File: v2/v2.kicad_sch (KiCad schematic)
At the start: 65 parts, among them J1 rBUSoutV, J10 mcuTIEout, J2 rBUSinV, J3 cTIEoutV, J4 cTIEinV, J5 cBUSoutH, J6 cTIEoutH, J7 mcuTIEin, J8 cTIEinH, J9 cBUSinH, SW1 KeySwitch, SW10 KeySwitch, SW11 KeySwitch, SW12 KeySwitch, SW13 KeySwitch, SW14 KeySwitch, SW15 KeySwitch, SW16 KeySwitch, SW17 KeySwitch, SW18 KeySwitch, SW19 KeySwitch, SW2 KeySwitch, SW20 KeySwitch, SW21 KeySwitch, SW22 KeySwitch, SW23 KeySwitch, SW24 KeySwitch, SW25 KeySwitch, SW3 KeySwitch, SW4 KeySwitch, SW5 KeySwitch, SW6 KeySwitch, SW7 KeySwitch, SW8 KeySwitch, SW9 KeySwitch, U1 ItsyBitsy5V

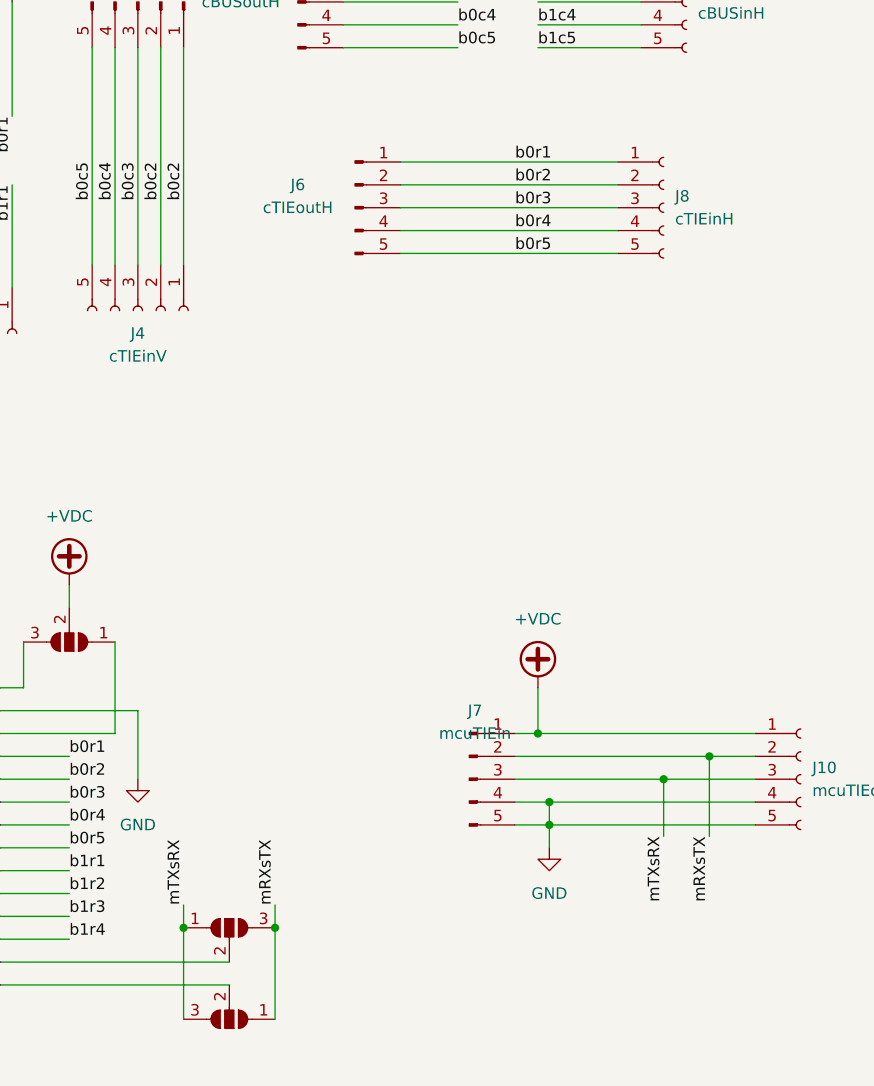
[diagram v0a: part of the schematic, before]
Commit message: Finish v2 keyboard tile
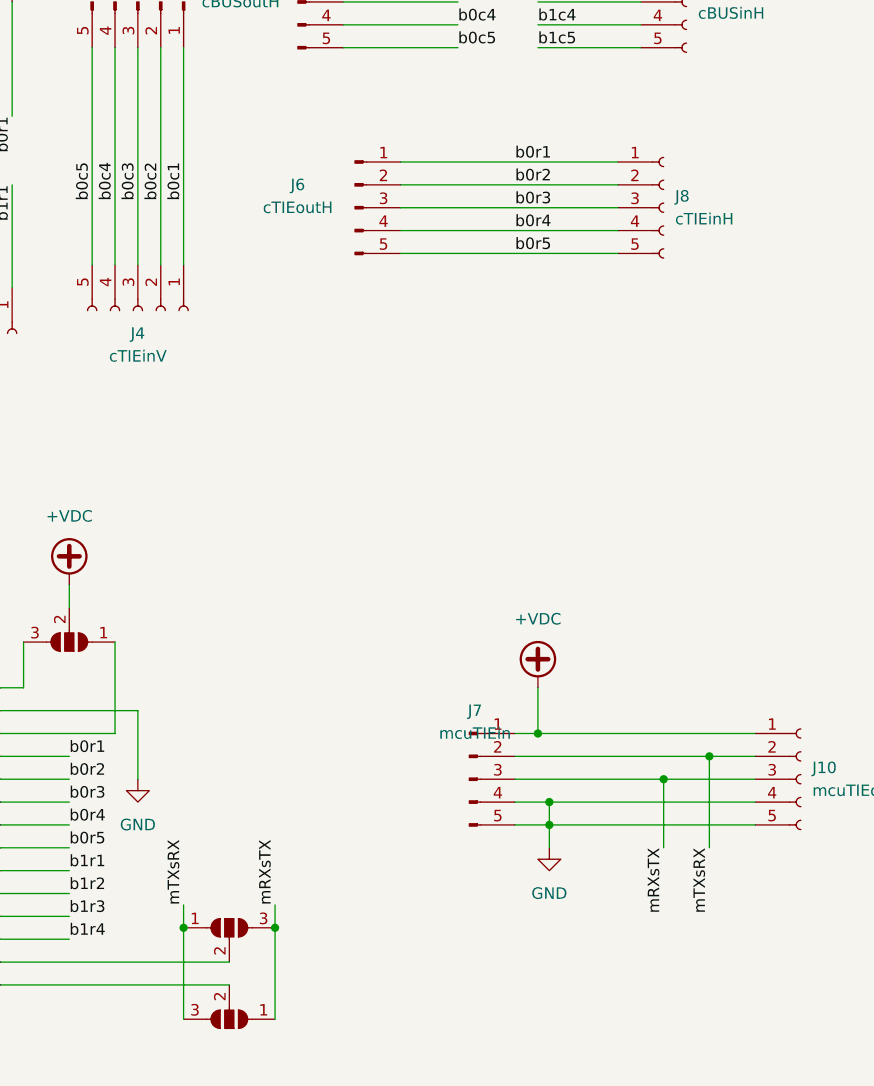
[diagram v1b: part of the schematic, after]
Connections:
- net b0c1: now also J3.1 (Pin_1), J4.1 (Pin_1)
- net b0c2: no longer J3.1 (Pin_1), J4.1 (Pin_1)
- net mRXsTX: now also J10.3 (Pin_3), J7.3 (Pin_3); no longer J10.2 (Pin_2), J7.2 (Pin_2)
- net mTXsRX: now also J10.2 (Pin_2), J7.2 (Pin_2); no longer J10.3 (Pin_3), J7.3 (Pin_3)
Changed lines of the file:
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@@
   (junction (at 95.25 83.82) (diameter 0) (color 0 0 0 0)
   )
-  (wire (pts (xy 144.78 215.9) (xy 144.78 222.25))
+  (wire (pts (xy 144.78 215.9) (xy 144.78 223.52))
     (stroke (width 0) (type default) (color 0 0 0 0))
   )
@@
     (stroke (width 0) (type default) (color 0 0 0 0))
   )
-  (wire (pts (xy 149.86 213.36) (xy 149.86 222.25))
+  (wire (pts (xy 149.86 213.36) (xy 149.86 223.52))
     (stroke (width 0) (type default) (color 0 0 0 0))
   )
@@
     (effects (font (size 1.27 1.27)) (justify left bottom))
   )
+  (label "mTXsRX" (at 149.86 223.52 270)
+    (effects (font (size 1.27 1.27)) (justify right bottom))
+  )
   (label "b0r3" (at 78.74 218.44 0)
     (effects (font (size 1.27 1.27)) (justify left bottom))
@@
     (effects (font (size 1.27 1.27)) (justify right bottom))
   )
+  (label "mRXsTX" (at 144.78 223.52 270)
+    (effects (font (size 1.27 1.27)) (justify right bottom))
+  )
   (label "b0c3" (at 111.76 101.6 0)
     (effects (font (size 1.27 1.27)) (justify left bottom))
   )
-  (label "mTXsRX" (at 144.78 222.25 270)
-    (effects (font (size 1.27 1.27)) (justify right bottom))
-  )
   (label "b0r2" (at 69.85 142.24 270)
     (effects (font (size 1.27 1.27)) (justify right bottom))
@@
     (effects (font (size 1.27 1.27)) (justify right bottom))
   )
-  (label "mRXsTX" (at 149.86 222.25 270)
-    (effects (font (size 1.27 1.27)) (justify right bottom))
-  )
   (label "b1r4" (at 78.74 233.68 0)
     (effects (font (size 1.27 1.27)) (justify left bottom))
@@
     (effects (font (size 1.27 1.27)) (justify left bottom))
   )
-  (label "b0c2" (at 91.44 147.32 270)
-    (effects (font (size 1.27 1.27)) (justify right bottom))
-  )
+  (label "b0c1" (at 91.44 147.32 270)
+    (effects (font (size 1.27 1.27)) (justify right bottom))
+  )

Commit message: Change diode to SOD-123, some tweaks
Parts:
- D1, D10, D11, D12, D13, D14, D15, D16, D17, D18, D19, D2, D20, D21, D22, D23, D24, D25, D3, D4, D5, D6, D7, D8, D9: footprint ProjectLibrary:D_0805_2012Metric_Pad1.15x1.40mm_HandSolder_No_Silk -> ProjectLibrary:D_SOD-123_NoSilk
